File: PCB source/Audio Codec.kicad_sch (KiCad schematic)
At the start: 35 parts, among them J3 JST XH, Q10 AO3401A, Q6 AO3401A, Q7 AO3400A, U8 TDA7052A, U9 PCM2704CDBR, X1 X322512MSB4SI

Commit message: production ready
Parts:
- removed Q10: AO3401A, PCM_JLCPCB:Q_SOT-23, symbol PCM_JLCPCB-Transistors:PMOS,AO3401A
- removed R55, R58: 10kΩ, PCM_JLCPCB:R_0402, symbol PCM_JLCPCB-Resistors:0402,10kΩ
- removed R60, R61: 22Ω, PCM_JLCPCB:R_0402, symbol PCM_JLCPCB-Resistors:0402,22Ω
- added R49: 22Ω, PCM_JLCPCB:R_0402, symbol PCM_JLCPCB-Resistors:0402,22Ω
- added R60: 10kΩ, PCM_JLCPCB:R_0402, symbol PCM_JLCPCB-Resistors:0402,10kΩ
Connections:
- net +5V: now also R49.2
- net DAC reset: now also R60.1
- net at C42.1, RV1.1, RV1.2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: now also R49.1
- net at Q6.1 (G): now also R60.2
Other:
- note added: "MAX POWER!"

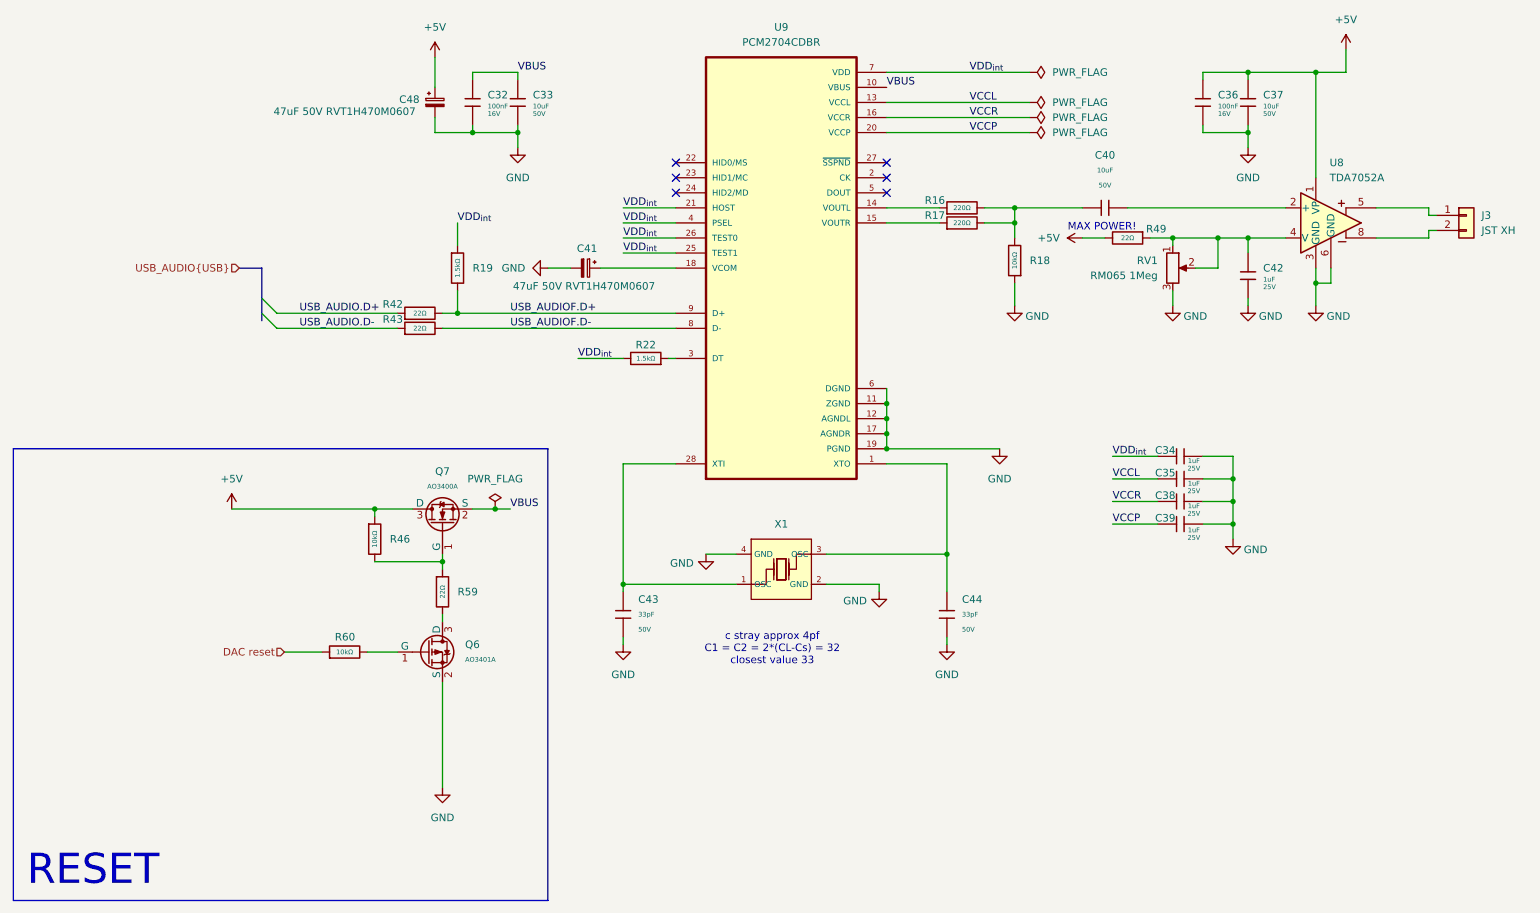
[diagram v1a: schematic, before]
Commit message: Fix can power delivery , fixed placment of the mosfets, CAN power  pull down to avoid DFU boot, added new porgraming connector
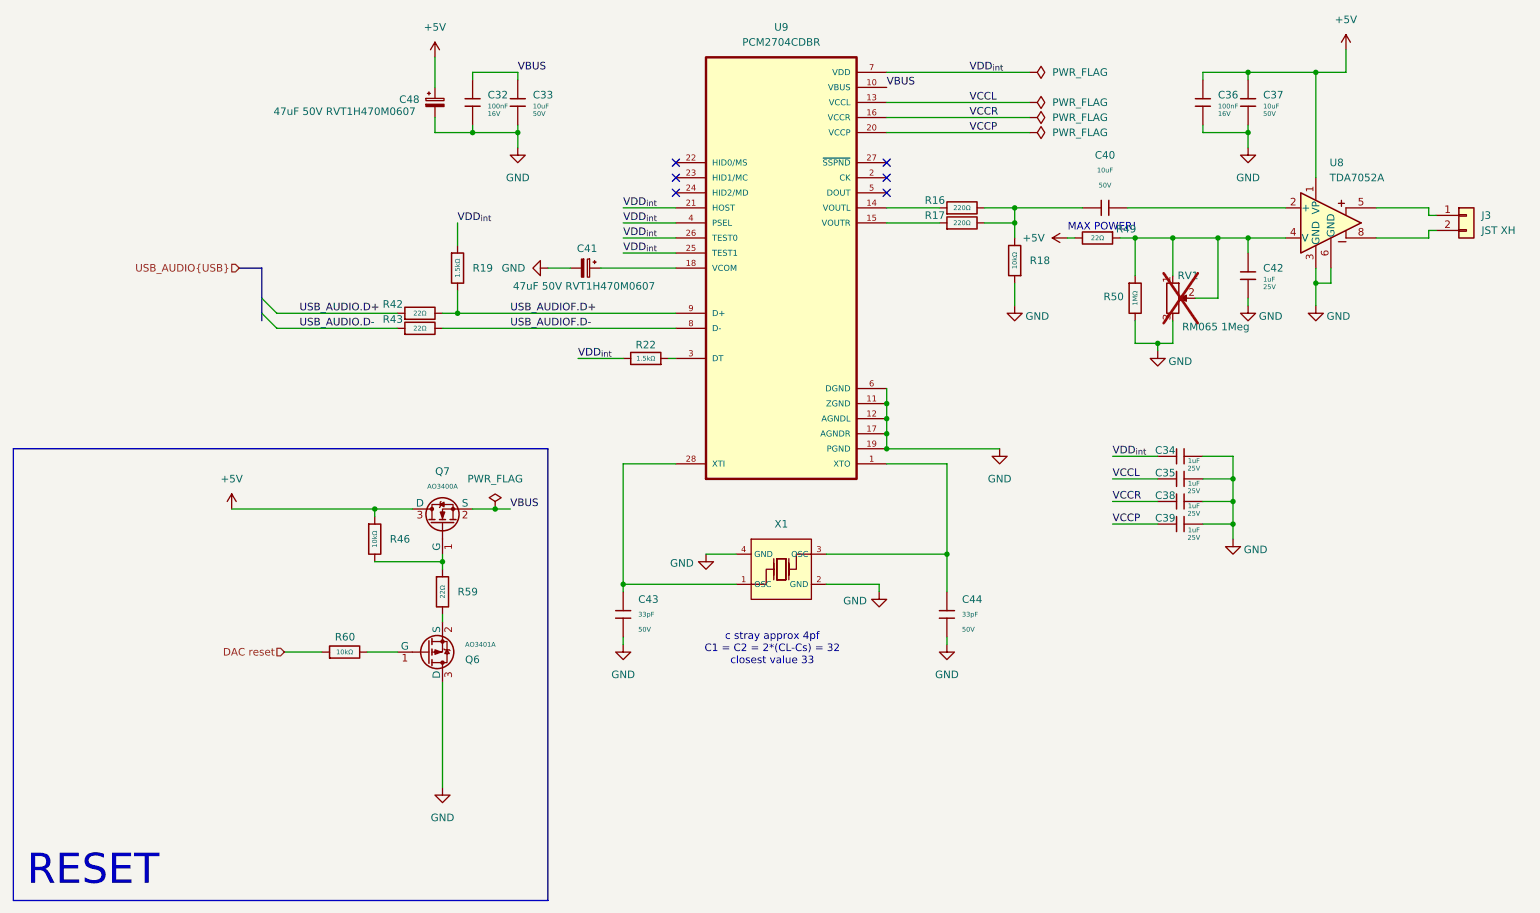
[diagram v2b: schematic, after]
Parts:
- added R50: 1MΩ, PCM_JLCPCB:R_0402, symbol PCM_JLCPCB-Resistors:0402,1MΩ
- RV1: now not fitted
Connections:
- net GND: now also Q6.3 (D), R50.2; no longer Q6.2 (S)
- net at C42.1, R49.1, RV1.1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: now also R50.1
- net at R59.2: now also Q6.2 (S); no longer Q6.3 (D)
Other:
- moved on the sheet: R49
